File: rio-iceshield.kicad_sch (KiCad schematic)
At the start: 43 parts, among them J2 Conn_01x06, J3 Conn_01x06, J4 Conn_01x06, J5 Conn_01x06, J6 Conn_01x06, J7 Conn_02x06_Odd_Even, U1 ICE40UP5K-SG48ITR, U2 AT25SF081-SSHF-X, U3 LD3985M122R_SOT23, U9 ULN2803A, X2 XO91, j1 GPIO

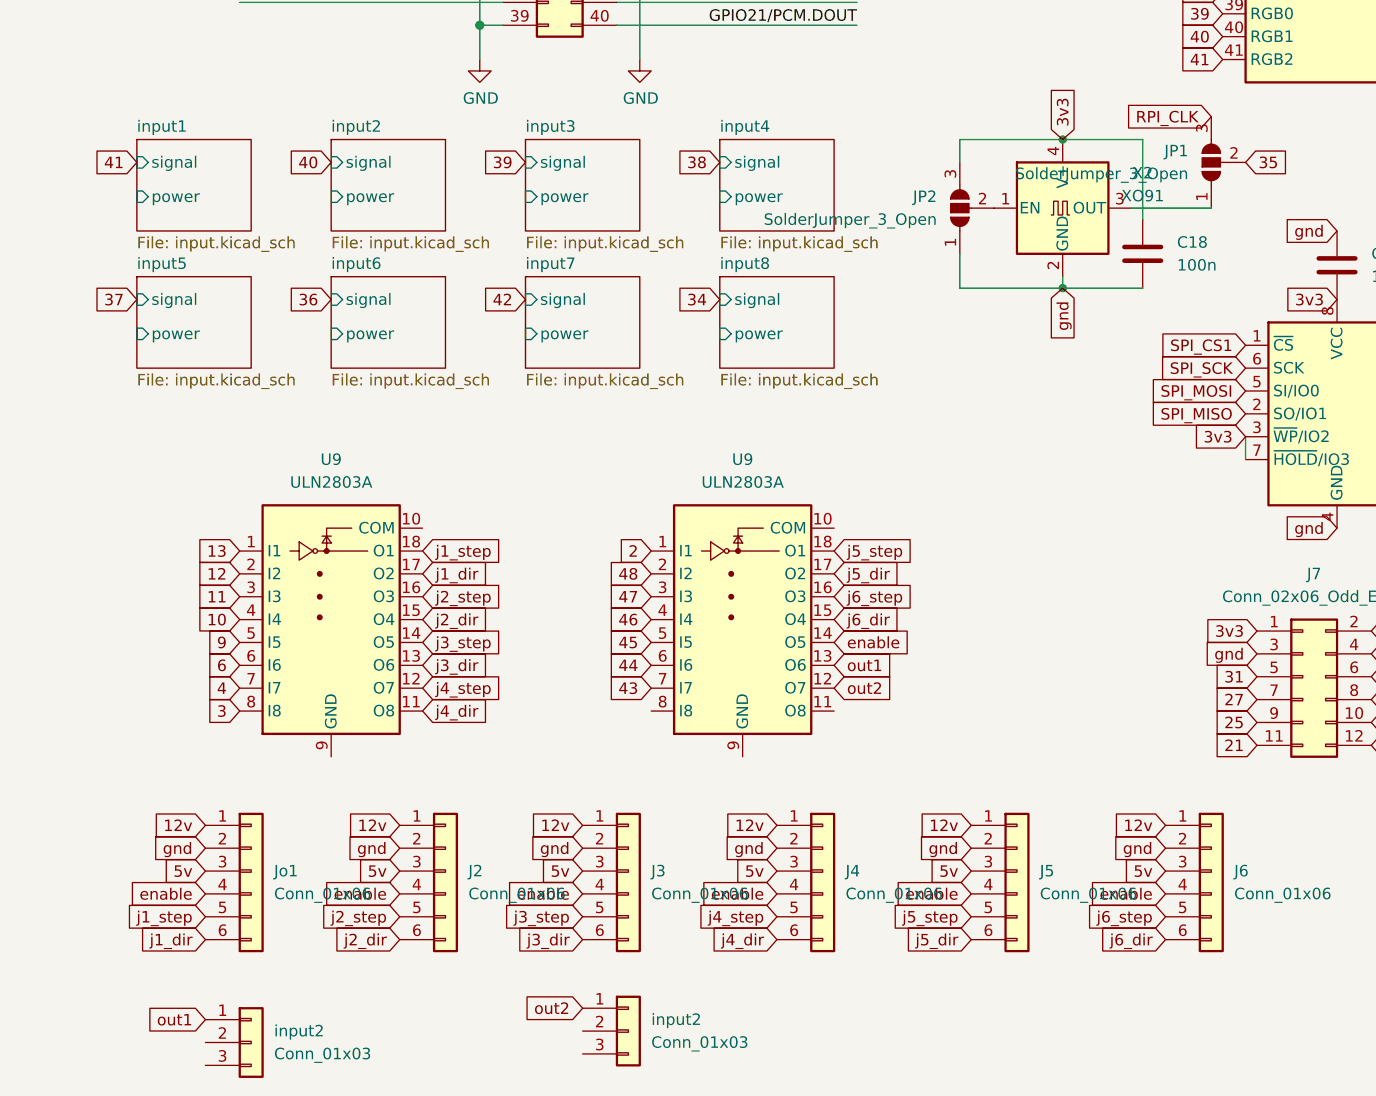
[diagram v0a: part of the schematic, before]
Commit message: adding missing in/out powerlines
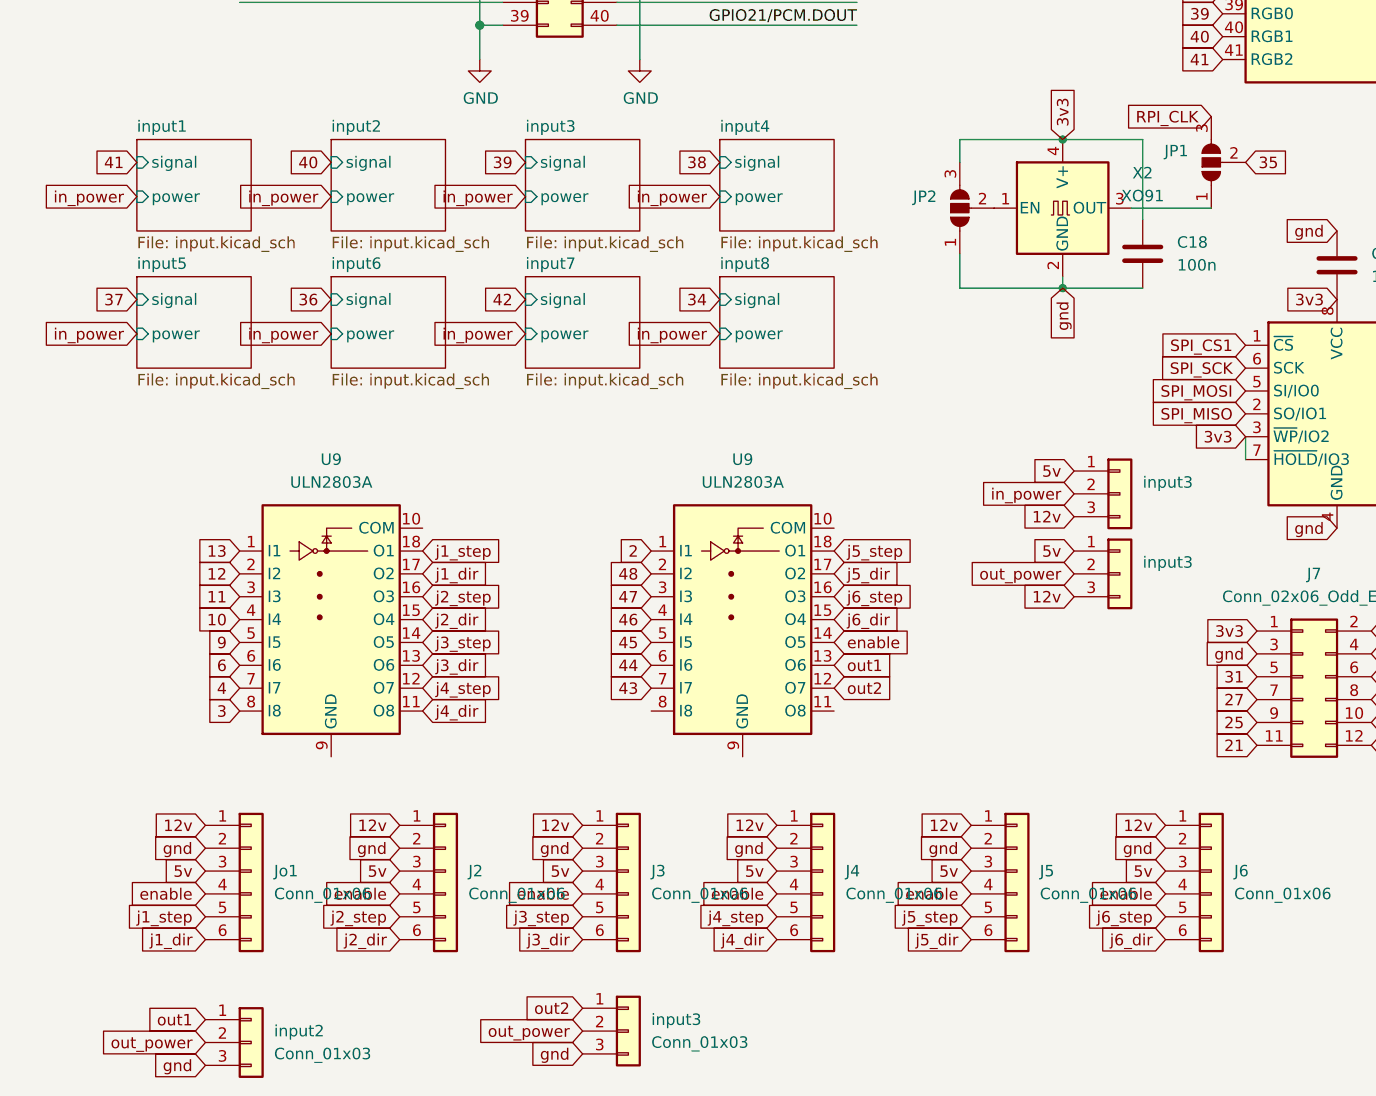
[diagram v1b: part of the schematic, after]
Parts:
- added input3 (x2): Conn_01x03, Connector_PinHeader_2.54mm:PinHeader_1x03_P2.54mm_Vertical, symbol Connector_Generic:Conn_01x03
- renumbered input2 to input3
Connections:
- net +5V: now also input3.1 (Pin_1), input3.1 (Pin_1)
- net 12v: now also input3.3 (Pin_3), input3.3 (Pin_3)
- net GND: now also input2.3 (Pin_3), input3.3 (Pin_3)
- net out_power: now reaches input3.2 (Pin_2)
- net out_power: now also input2.2 (Pin_2), input3.2 (Pin_2)
- new net in_power: input3.2 (Pin_2)

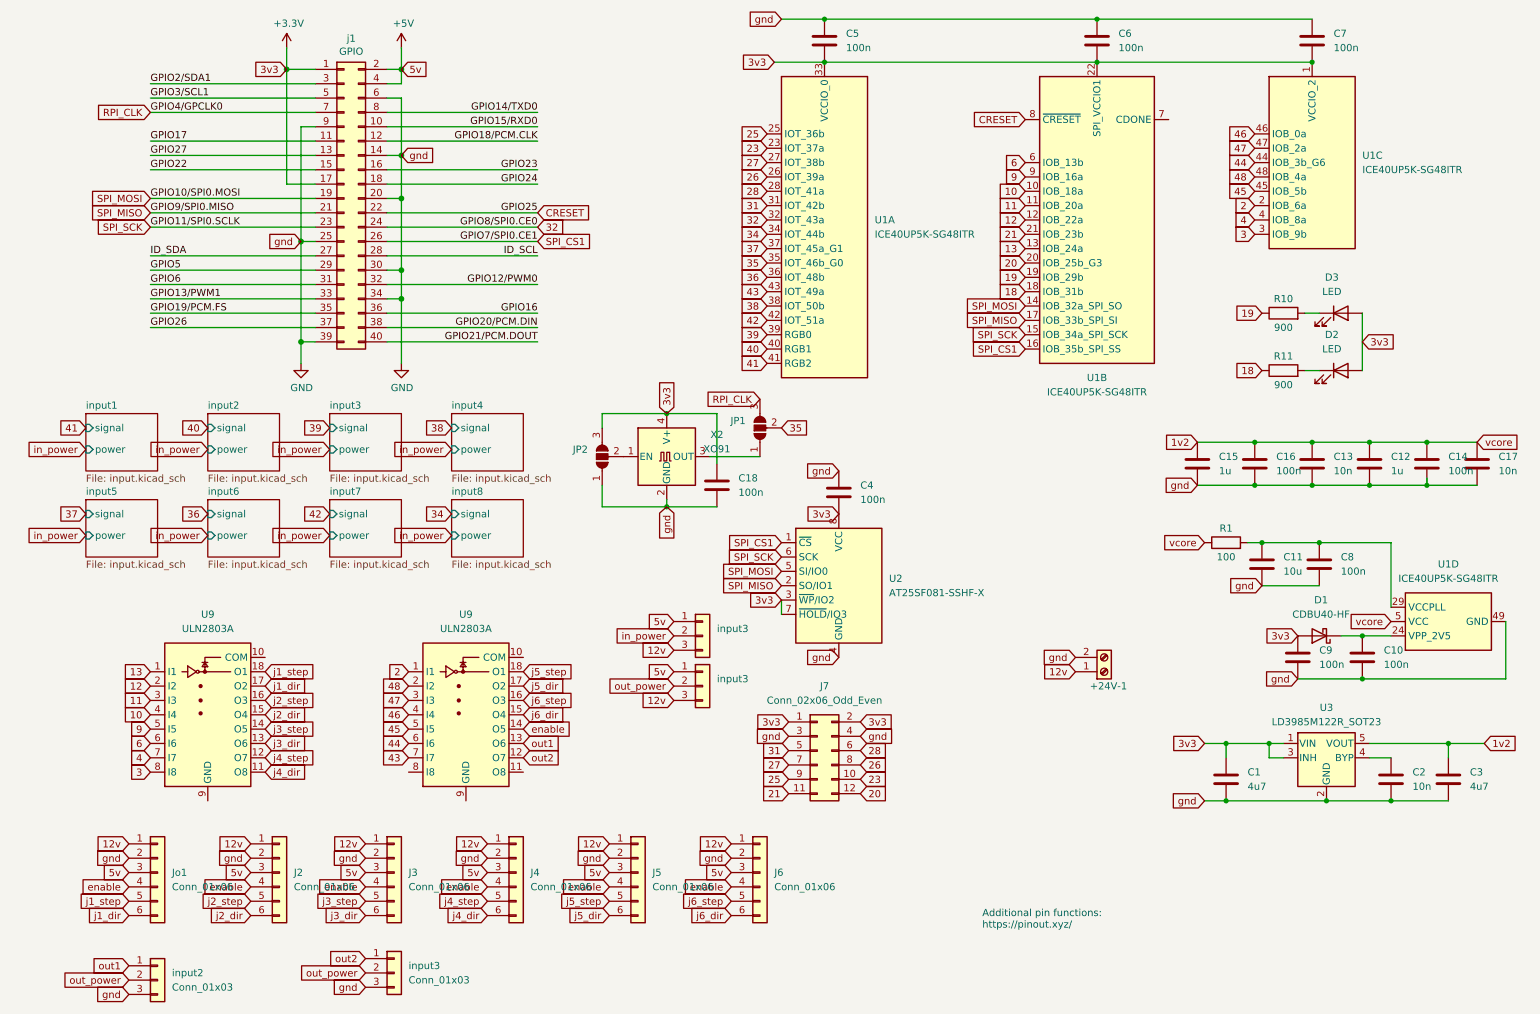
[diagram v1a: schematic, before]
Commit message: replacing spi-flash package
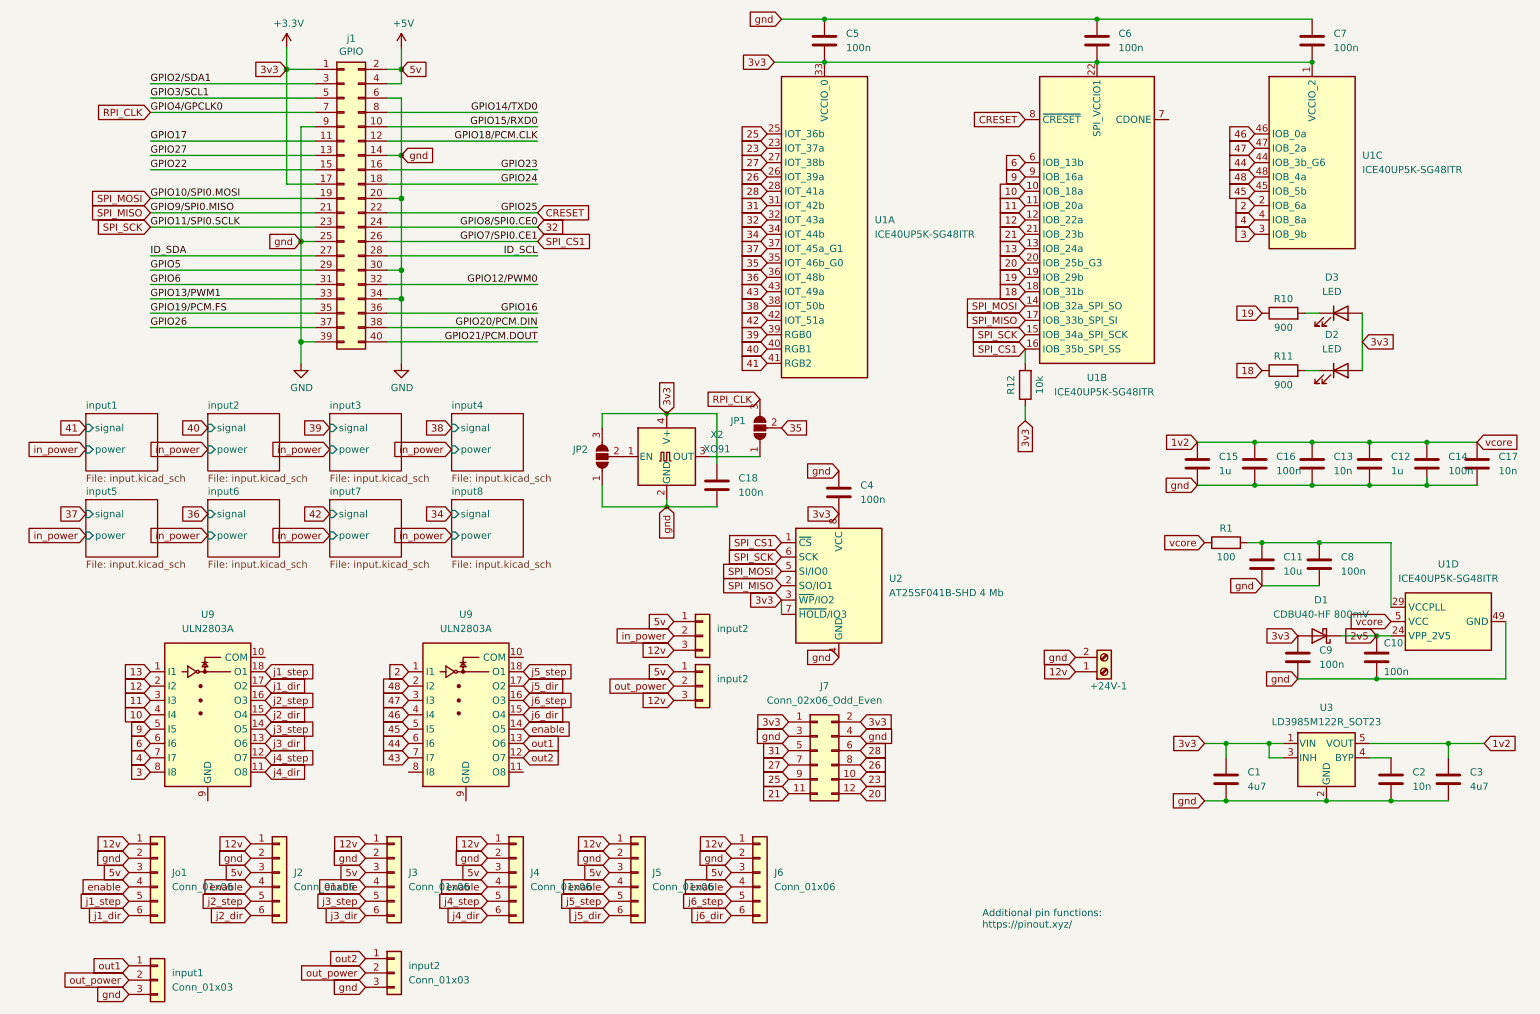
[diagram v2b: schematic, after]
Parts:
- added R12: 10k, Resistor_SMD:R_0805_2012Metric_Pad1.20x1.40mm_HandSolder, symbol Device:R
- D1: value CDBU40-HF -> CDBU40-HF 800mV
- U2: value AT25SF081-SSHF-X -> AT25SF041B-SHD 4 Mb; footprint Package_SO:SOIC-8_3.9x4.9mm_P1.27mm -> Package_SO:SOIC-8W_5.3x5.3mm_P1.27mm
- renumbered input2 to input1, input3 to input2
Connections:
- net +3V3: now also R12.1
- net SPI_CS1: now also R12.2
- net 2v5: now reaches C10.1, D1.1 (K), U1.24 (VPP_2V5)
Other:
- moved on the sheet: C10

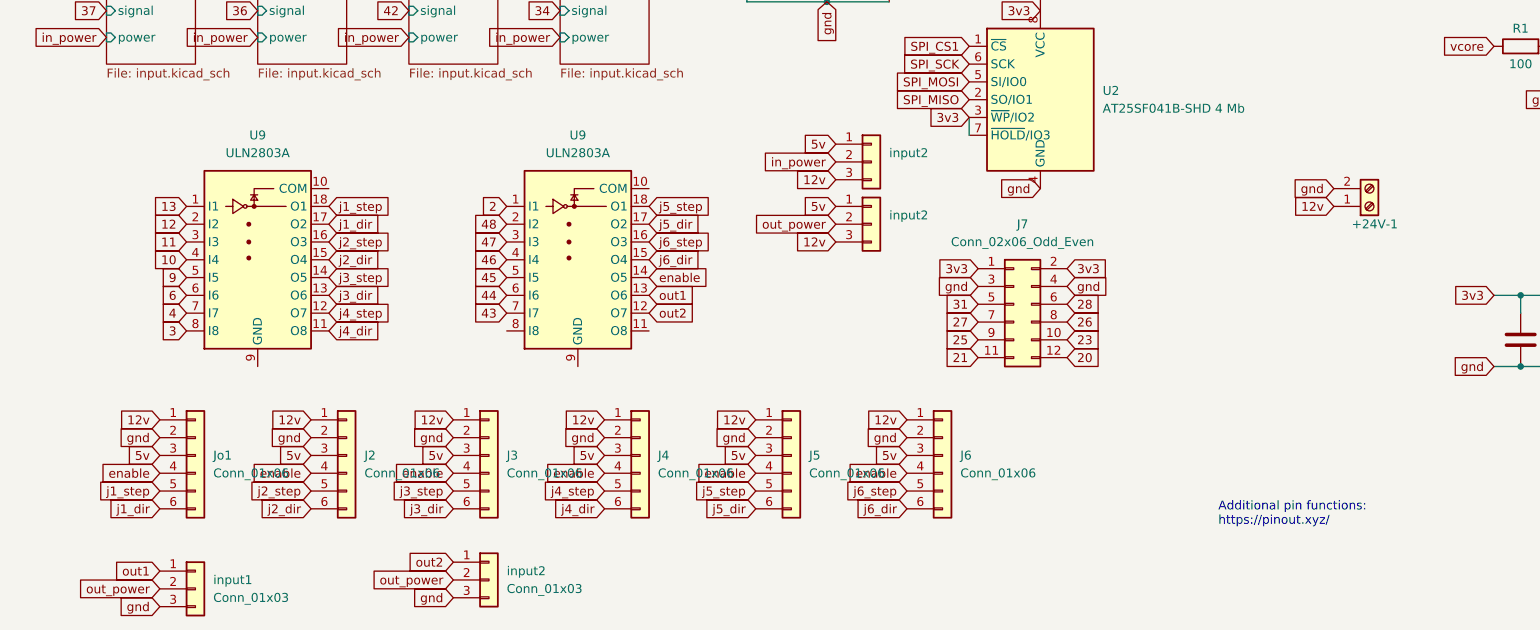
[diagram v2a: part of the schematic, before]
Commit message: adding pulldowns to outputs / fixing uln gnd's
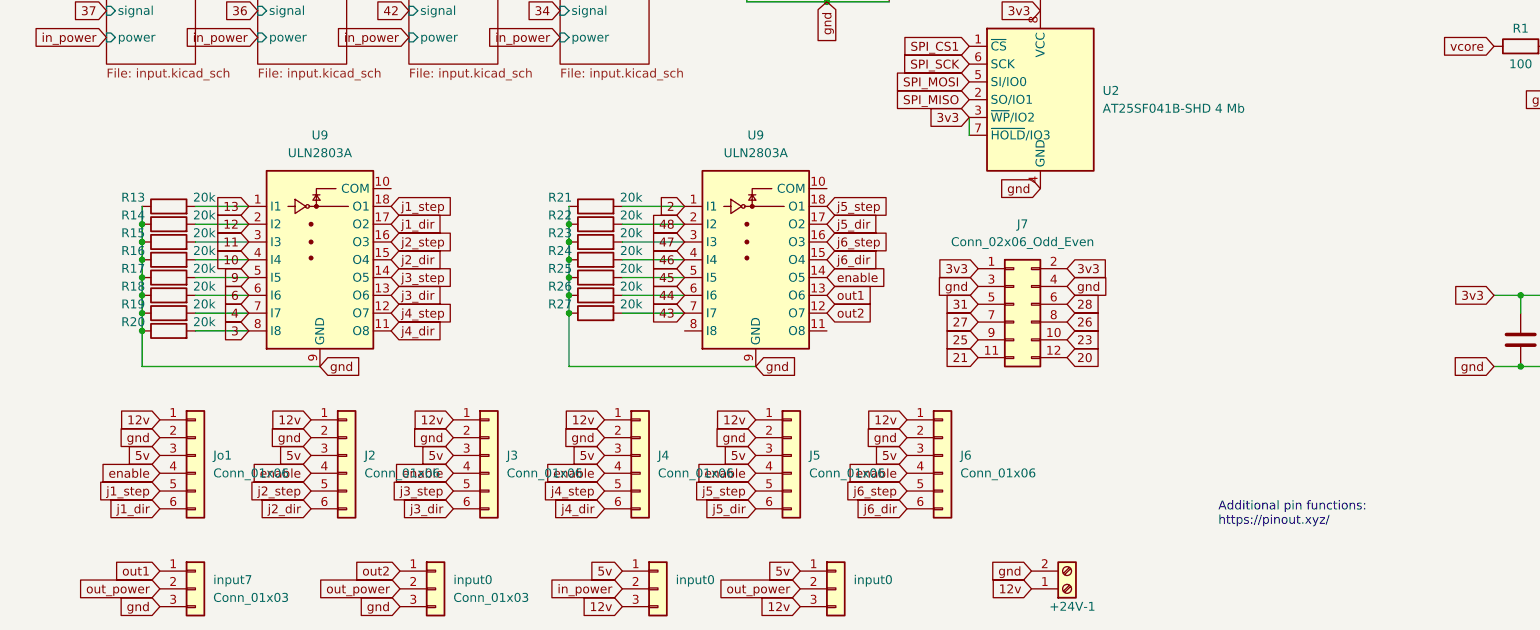
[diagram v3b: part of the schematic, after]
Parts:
- added R13, R14, R15, R16, R17, R18, R19, R20, R21, R22, R23, R24, R25, R26, R27: 20k, Resistor_SMD:R_0805_2012Metric_Pad1.20x1.40mm_HandSolder, symbol Device:R
- renumbered input2 to input0, input1 to input7
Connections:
- net 10: now also R16.2
- net 11: now also R15.2
- net 12: now also R14.2
- net 13: now also R13.2
- net 2: now also R21.2
- net 3: now also R20.2
- net 4: now also R19.2
- net 43: now also R27.2
- net 44: now also R26.2
- net 45: now also R25.2
- net 46: now also R24.2
- net 47: now also R23.2
- net 48: now also R22.2
- net 6: now also R18.2
- net 9: now also R17.2
- net GND: now also U9.9 (GND), U9.9 (GND), R13.1, R14.1, R15.1, R16.1, R17.1, R18.1, R19.1, R20.1, R21.1, R22.1, R23.1, R24.1, R25.1, R26.1, R27.1
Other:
- moved on the sheet: +24V-1, U9, input0
